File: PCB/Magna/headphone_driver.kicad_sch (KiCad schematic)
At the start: 36 parts, among them J1201 AudioJack3, U1201 NE5532, U1202 NE5532

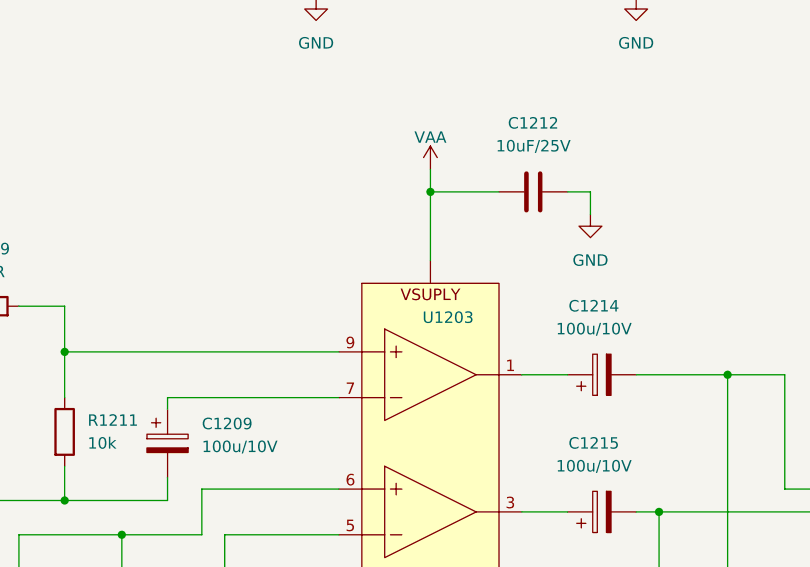
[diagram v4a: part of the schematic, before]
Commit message: Select parts for all components
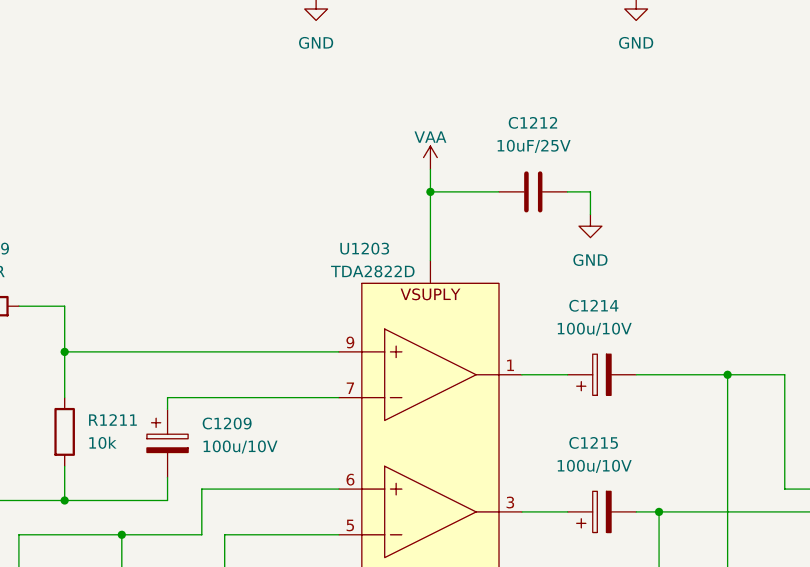
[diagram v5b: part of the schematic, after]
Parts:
- J1201: footprint (none) -> Connector_Audio:Jack_3.5mm_CUI_SJ1-3525N_Horizontal; LCSC (none) -> C668604
- R1201, R1202, R1207, R1208: footprint (none) -> Resistor_SMD:R_0805_2012Metric; LCSC (none) -> C479095
- R1203, R1204: footprint (none) -> Resistor_SMD:R_0805_2012Metric_Pad1.20x1.40mm_HandSolder; LCSC (none) -> C865612
- R1205, R1206: footprint (none) -> Resistor_SMD:R_0805_2012Metric_Pad1.20x1.40mm_HandSolder; LCSC (none) -> C218394
- R1209, R1210: footprint (none) -> Resistor_SMD:R_0805_2012Metric_Pad1.20x1.40mm_HandSolder; LCSC (none) -> C217766
- R1211, R1212: footprint (none) -> Resistor_SMD:R_0805_2012Metric; LCSC (none) -> C17414
- R1213, R1214: footprint (none) -> Resistor_SMD:R_0805_2012Metric_Pad1.20x1.40mm_HandSolder; LCSC (none) -> C2683106
- U1201, U1202: LCSC (none) -> C7426
- U1203: value ~ -> TDA2822D; LCSC (none) -> C5145398
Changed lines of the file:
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@@
       (effects (font (size 1.27 1.27)) (justify right))
     )
-    (property "Footprint" "" (at 271.78 104.14 0)
+    (property "Footprint" "Connector_Audio:Jack_3.5mm_CUI_SJ1-3525N_Horizontal" (at 271.78 104.14 0)
       (effects (font (size 1.27 1.27)) hide)
     )
     (property "Datasheet" "~" (at 271.78 104.14 0)
+      (effects (font (size 1.27 1.27)) hide)
+    )
+    (property "LCSC" "C668604" (at 271.78 104.14 0)
       (effects (font (size 1.27 1.27)) hide)
     )
@@
       (effects (font (size 1.27 1.27)) (justify left))
     )
-    (property "Footprint" "" (at 56.642 82.55 90)
+    (property "Footprint" "Resistor_SMD:R_0805_2012Metric" (at 56.642 82.55 90)
       (effects (font (size 1.27 1.27)) hide)
     )
@@
       (effects (font (size 1.27 1.27)) hide)
     )
+    (property "LCSC" "C479095" (at 58.42 82.55 0)
+      (effects (font (size 1.27 1.27)) hide)
+    )
     (pin "2")
     (pin "1")
@@
     )
     (property "Datasheet" "http://www.ti.com/lit/ds/symlink/ne5532.pdf" (at 88.9 78.74 0)
+      (effects (font (size 1.27 1.27)) hide)
+    )
+    (property "LCSC" "C7426" (at 88.9 78.74 0)
       (effects (font (size 1.27 1.27)) hide)
     )
@@
       (effects (font (size 1.27 1.27)))
     )
-    (property "Footprint" "" (at 110.49 152.908 90)
+    (property "Footprint" "Resistor_SMD:R_0805_2012Metric_Pad1.20x1.40mm_HandSolder" (at 110.49 152.908 90)
       (effects (font (size 1.27 1.27)) hide)
     )
     (property "Datasheet" "~" (at 110.49 151.13 0)
+      (effects (font (size 1.27 1.27)) hide)
+    )
+    (property "LCSC" "C865612" (at 110.49 151.13 0)
       (effects (font (size 1.27 1.27)) hide)
     )
@@
     )
     (property "Datasheet" "http://www.ti.com/lit/ds/symlink/ne5532.pdf" (at 134.62 153.67 0)
+      (effects (font (size 1.27 1.27)) hide)
+    )
+    (property "LCSC" "C7426" (at 134.62 153.67 0)
       (effects (font (size 1.27 1.27)) hide)
     )
@@
       (effects (font (size 1.27 1.27)) (justify left))
     )
-    (property "Footprint" "" (at 163.322 87.63 90)
+    (property "Footprint" "Resistor_SMD:R_0805_2012Metric" (at 163.322 87.63 90)
       (effects (font (size 1.27 1.27)) hide)
     )
@@
       (effects (font (size 1.27 1.27)) hide)
     )
+    (property "LCSC" "C479095" (at 165.1 87.63 0)
+      (effects (font (size 1.27 1.27)) hide)
+    )
     (pin "2")
     (pin "1")
@@
       (effects (font (size 1.27 1.27)) (justify left))
     )
-    (property "Footprint" "" (at 163.322 160.02 90)
+    (property "Footprint" "Resistor_SMD:R_0805_2012Metric" (at 163.322 160.02 90)
       (effects (font (size 1.27 1.27)) hide)
     )
     (property "Datasheet" "~" (at 165.1 160.02 0)
+      (effects (font (size 1.27 1.27)) hide)
+    )
+    (property "LCSC" "C479095" (at 165.1 160.02 0)
       (effects (font (size 1.27 1.27)) hide)
     )
@@
       (effects (font (size 1.27 1.27)))
     )
-    (property "Footprint" "" (at 171.45 155.448 90)
+    (property "Footprint" "Resistor_SMD:R_0805_2012Metric_Pad1.20x1.40mm_HandSolder" (at 171.45 155.448 90)
       (effects (font (size 1.27 1.27)) hide)
     )
@@
       (effects (font (size 1.27 1.27)) hide)
     )
+    (property "LCSC" "C217766" (at 171.45 153.67 0)
+      (effects (font (size 1.27 1.27)) hide)
+    )
     (pin "1")
     (pin "2")
@@
       (effects (font (size 1.27 1.27)) (justify left))
     )
-    (property "Footprint" "" (at 184.912 115.57 90)
+    (property "Footprint" "Resistor_SMD:R_0805_2012Metric" (at 184.912 115.57 90)
       (effects (font (size 1.27 1.27)) hide)
     )
     (property "Datasheet" "~" (at 186.69 115.57 0)
+      (effects (font (size 1.27 1.27)) hide)
+    )
+    (property "LCSC" "C17414" (at 186.69 115.57 0)
       (effects (font (size 1.27 1.27)) hide)
     )
@@
       (effects (font (size 1.27 1.27)))
     )
-    (property "Footprint" "" (at 171.45 83.058 90)
+    (property "Footprint" "Resistor_SMD:R_0805_2012Metric_Pad1.20x1.40mm_HandSolder" (at 171.45 83.058 90)
       (effects (font (size 1.27 1.27)) hide)
     )
@@
       (effects (font (size 1.27 1.27)) hide)
     )
+    (property "LCSC" "C217766" (at 171.45 81.28 0)
+      (effects (font (size 1.27 1.27)) hide)
+    )
     (pin "1")
     (pin "2")
@@
       (effects (font (size 1.27 1.27)) (justify left))
     )
-    (property "Footprint" "" (at 56.642 154.94 90)
+    (property "Footprint" "Resistor_SMD:R_0805_2012Metric" (at 56.642 154.94 90)
       (effects (font (size 1.27 1.27)) hide)
     )
@@
       (effects (font (size 1.27 1.27)) hide)
     )
+    (property "LCSC" "C479095" (at 58.42 154.94 0)
+      (effects (font (size 1.27 1.27)) hide)
+    )
     (pin "2")
     (pin "1")
@@
       (effects (font (size 1.27 1.27)))
     )
-    (property "Footprint" "" (at 133.35 140.208 90)
+    (property "Footprint" "Resistor_SMD:R_0805_2012Metric_Pad1.20x1.40mm_HandSolder" (at 133.35 140.208 90)
       (effects (font (size 1.27 1.27)) hide)
     )
     (property "Datasheet" "~" (at 133.35 138.43 0)
+      (effects (font (size 1.27 1.27)) hide)
+    )
+    (property "LCSC" "C218394" (at 133.35 138.43 0)
       (effects (font (size 1.27 1.27)) hide)
     )
@@
     )
     (property "Datasheet" "http://www.ti.com/lit/ds/symlink/ne5532.pdf" (at 134.62 81.28 0)
+      (effects (font (size 1.27 1.27)) hide)
+    )
+    (property "LCSC" "C7426" (at 134.62 81.28 0)
       (effects (font (size 1.27 1.27)) hide)
     )
@@
       (effects (font (size 1.27 1.27)) (justify left))
     )
-    (property "Footprint" "" (at 248.158 142.24 90)
+    (property "Footprint" "Resistor_SMD:R_0805_2012Metric_Pad1.20x1.40mm_HandSolder" (at 248.158 142.24 90)
       (effects (font (size 1.27 1.27)) hide)
     )
     (property "Datasheet" "~" (at 246.38 142.24 0)
+      (effects (font (size 1.27 1.27)) hide)
+    )
+    (property "LCSC" "C2683106" (at 246.38 142.24 0)
       (effects (font (size 1.27 1.27)) hide)
     )
@@
     )
     (property "Datasheet" "http://www.ti.com/lit/ds/symlink/ne5532.pdf" (at 246.38 34.29 0)
+      (effects (font (size 1.27 1.27)) hide)
+    )
+    (property "LCSC" "C7426" (at 246.38 34.29 0)
       (effects (font (size 1.27 1.27)) hide)
     )
@@
       (effects (font (size 1.27 1.27)))
     )
-    (property "Footprint" "" (at 133.35 67.818 90)
+    (property "Footprint" "Resistor_SMD:R_0805_2012Metric_Pad1.20x1.40mm_HandSolder" (at 133.35 67.818 90)
       (effects (font (size 1.27 1.27)) hide)
     )
@@
       (effects (font (size 1.27 1.27)) hide)
     )
+    (property "LCSC" "C218394" (at 133.35 66.04 0)
+      (effects (font (size 1.27 1.27)) hide)
+    )
     (pin "1")
     (pin "2")
@@
       (effects (font (size 1.27 1.27)) (justify left))
     )
-    (property "Footprint" "" (at 252.222 142.24 90)
+    (property "Footprint" "Resistor_SMD:R_0805_2012Metric_Pad1.20x1.40mm_HandSolder" (at 252.222 142.24 90)
       (effects (font (size 1.27 1.27)) hide)
     )
@@
       (effects (font (size 1.27 1.27)) hide)
     )
+    (property "LCSC" "C2683106" (at 254 142.24 0)
+      (effects (font (size 1.27 1.27)) hide)
+    )
     (pin "1")
     (pin "2")
@@
       (effects (font (size 1.27 1.27)) (justify left))
     )
-    (property "Footprint" "" (at 178.562 95.25 90)
+    (property "Footprint" "Resistor_SMD:R_0805_2012Metric" (at 178.562 95.25 90)
       (effects (font (size 1.27 1.27)) hide)
     )
     (property "Datasheet" "~" (at 180.34 95.25 0)
+      (effects (font (size 1.27 1.27)) hide)
+    )
+    (property "LCSC" "C17414" (at 180.34 95.25 0)
       (effects (font (size 1.27 1.27)) hide)
     )
@@
     )
     (property "Datasheet" "http://www.ti.com/lit/ds/symlink/ne5532.pdf" (at 210.82 34.29 0)
+      (effects (font (size 1.27 1.27)) hide)
+    )
+    (property "LCSC" "C7426" (at 210.82 34.29 0)
       (effects (font (size 1.27 1.27)) hide)
     )
@@
   )
   (symbol (lib_id "Skrooter_symbols:TDA2822D") (at 213.36 86.36 0) (unit 1)
-    (in_bom yes) (on_board yes) (dnp no) (fields_autoplaced)
-    (property "Reference" "U1203" (at 220.0911 82.55 0)
-      (effects (font (size 1.27 1.27)) (justify left))
-    )
-    (property "Value" "~" (at 213.36 86.36 0)
+    (in_bom yes) (on_board yes) (dnp no)
+    (property "Reference" "U1203" (at 210.82 74.93 0)
+      (effects (font (size 1.27 1.27)) (justify left))
+    )
+    (property "Value" "TDA2822D" (at 214.63 77.47 0)
       (effects (font (size 1.27 1.27)))
     )
@@
     )
     (property "Datasheet" "" (at 213.36 86.36 0)
+      (effects (font (size 1.27 1.27)) hide)
+    )
+    (property "LCSC" "C5145398" (at 213.36 86.36 0)
       (effects (font (size 1.27 1.27)) hide)
     )
@@
       (effects (font (size 1.27 1.27)))
     )
-    (property "Footprint" "" (at 110.49 80.518 90)
+    (property "Footprint" "Resistor_SMD:R_0805_2012Metric_Pad1.20x1.40mm_HandSolder" (at 110.49 80.518 90)
       (effects (font (size 1.27 1.27)) hide)
     )
@@
       (effects (font (size 1.27 1.27)) hide)
     )
+    (property "LCSC" "C865612" (at 110.49 78.74 0)
+      (effects (font (size 1.27 1.27)) hide)
+    )
     (pin "2")
     (pin "1")
@@
       (effects (font (size 1.27 1.27)) hide)
     )
+    (property "LCSC" "C7426" (at 88.9 151.13 0)
+      (effects (font (size 1.27 1.27)) hide)
+    )
